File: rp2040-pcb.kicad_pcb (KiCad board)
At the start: 2 copper layers, 23.2 x 51.2 mm, 43 parts, among them J1 Conn_01x20_Male, J2 Conn_01x20_Male, J3 TYPE-C-31-M-12, SW1 SW_Push, SW2 SW_Push, U1 RP2040, U2 TPS54202DDC, U3 W25Q128JVSIQ, Y1 12 MHz

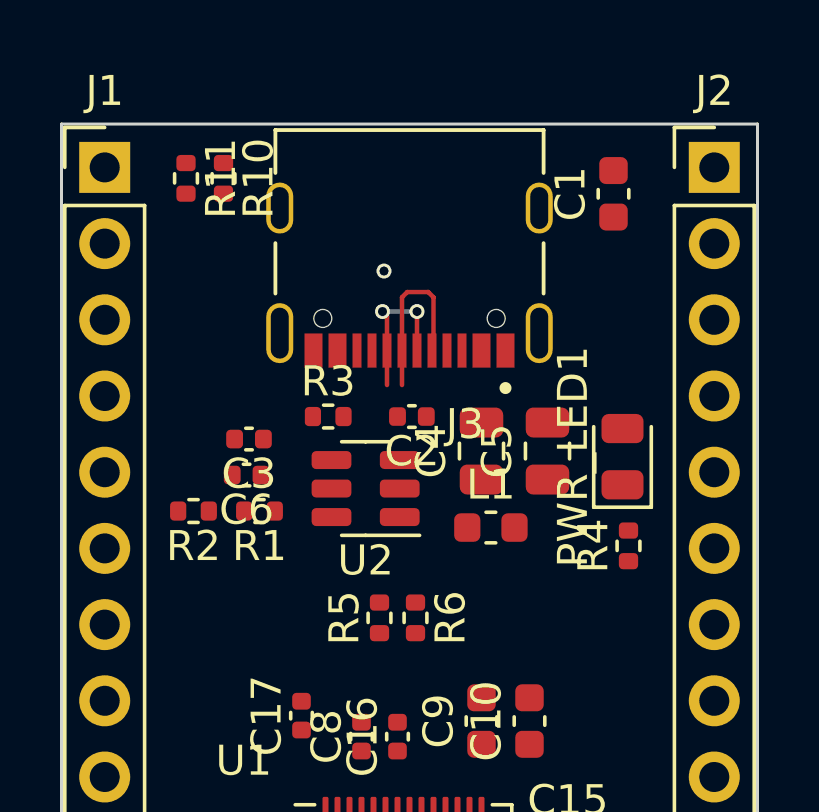
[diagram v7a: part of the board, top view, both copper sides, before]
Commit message: Routed voltage regulator.
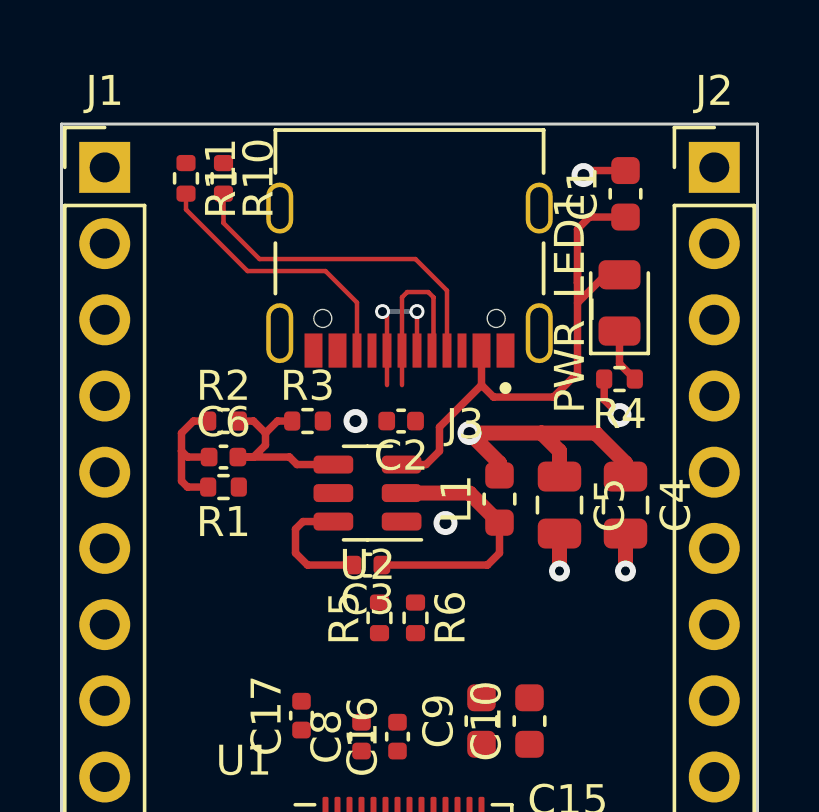
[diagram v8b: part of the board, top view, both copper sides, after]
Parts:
- moved C3 5.77 mm to (100.2, 92.0)
- moved R4 5.57 mm to (108.6, 85.8), turned to 180 degrees
- moved C4 5.13 mm to (108.8, 90.0), turned to -90 degrees
- moved PWR_LED1 5.13 mm to (108.6, 83.3)
- moved R2 3.16 mm to (95.4, 87.2), turned to 0 degrees
- moved C5 1.84 mm to (106.6, 90.0), turned to -90 degrees
- moved R1 1.44 mm to (95.4, 89.4)
- moved L1 0.99 mm to (104.6, 89.8), turned to 90 degrees
- moved C6 0.98 mm to (95.4, 88.4), turned to 0 degrees
- moved R3 0.71 mm to (98.2, 87.2)
- moved C1 0.40 mm to (108.8, 79.6)
- moved C2 0.39 mm to (101.3, 87.2)
- moved U2 0.16 mm to (100.2, 89.6)
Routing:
- net VCC: track 0.00 -> 17.8 mm
- net Net-(R10-Pad2): track 0.00 -> 11.4 mm, vias 1 -> 0
- net +3.3V: track 0.00 -> 9.59 mm, vias 0 -> 1
- net Net-(R11-Pad2): track 0.00 -> 9.11 mm
- net Net-(C3-Pad1): track 0.00 -> 8.77 mm
- net Net-(C6-Pad2): track 0.00 -> 6.88 mm
- net GND: track 0.00 -> 5.37 mm, vias 0 -> 4
- net Net-(C6-Pad1): track 0.00 -> 4.63 mm
- net Net-(C3-Pad2): track 0.00 -> 4.25 mm
- net Net-(PWR_LED1-Pad1): track 0.00 -> 1.81 mm
- net (no net): vias 0 -> 2
